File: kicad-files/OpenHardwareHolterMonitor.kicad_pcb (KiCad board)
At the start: 6 copper layers, 131 x 80 mm, 151 parts, among them CON1 Micro_SD_Card, J1 Conn_02x06_Odd_Even, J10 Conn_01x01, J11 Conn_01x01, J12 USB_OTG, J13 USB_C_Receptacle, J2 Conn_01x01, J3 Conn_01x01, J4 Conn_01x01, J5 Conn_01x01, J6 Conn_01x01, J7 Conn_01x01, J8 Conn_01x01, J9 Conn_01x01, P1 Custom_FTDI, Q1 S8050, Q10 Q_PMOS_DGS, Q2 S8050, Q3 Q_NMOS_DGS, Q4 Q_NMOS_DGS, Q5 Q_NMOS_DGS, Q6 Q_NMOS_DGS, Q7 Q_PMOS_DGS, Q8 Q_PMOS_DGS, Q9 Q_PMOS_DGS, SW1 SW_SPDT, U1 ESP-WROOM-32, U2 ADS1298, U3 MCP73833, U4 MCP73833, U5 TPS2113A, U6 LP5912, U7 REM_3-xxxxS, Y1 32768Hz

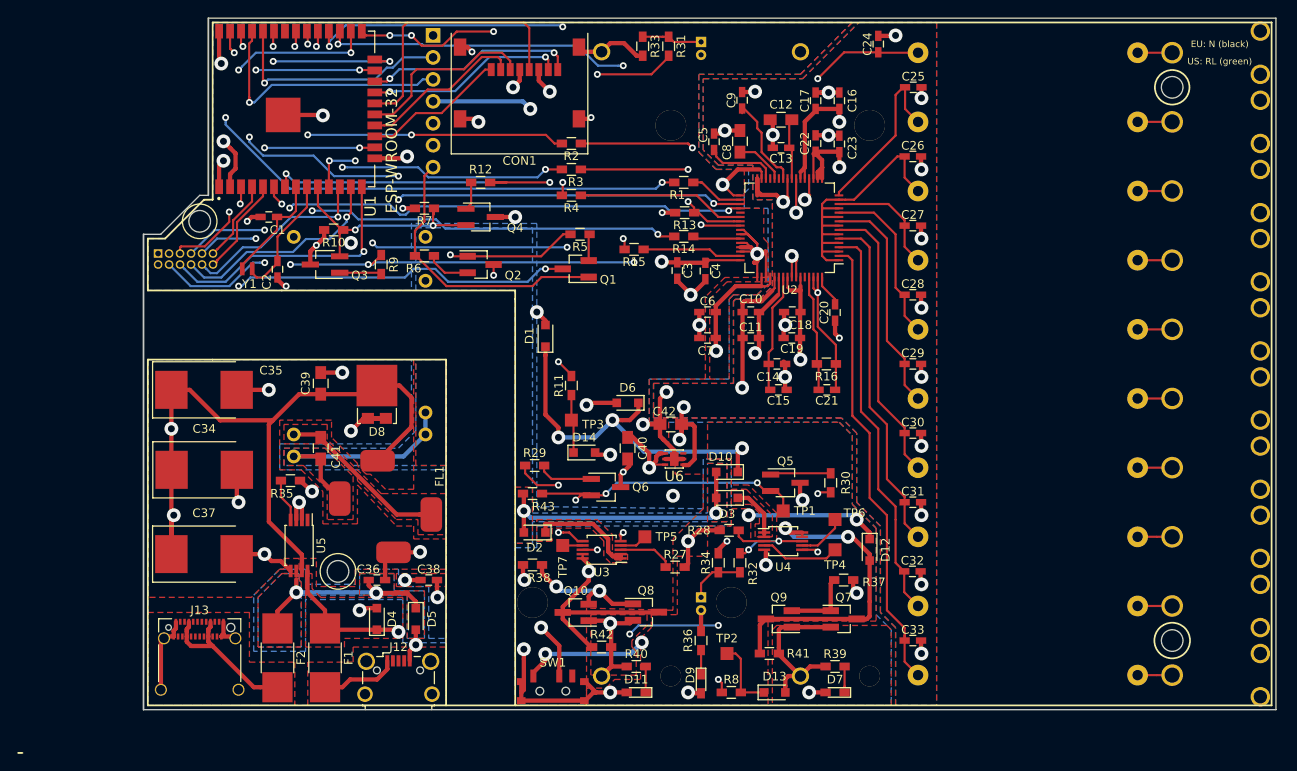
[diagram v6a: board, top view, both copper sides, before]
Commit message: DRC passes (with some missing courtyard warnings)
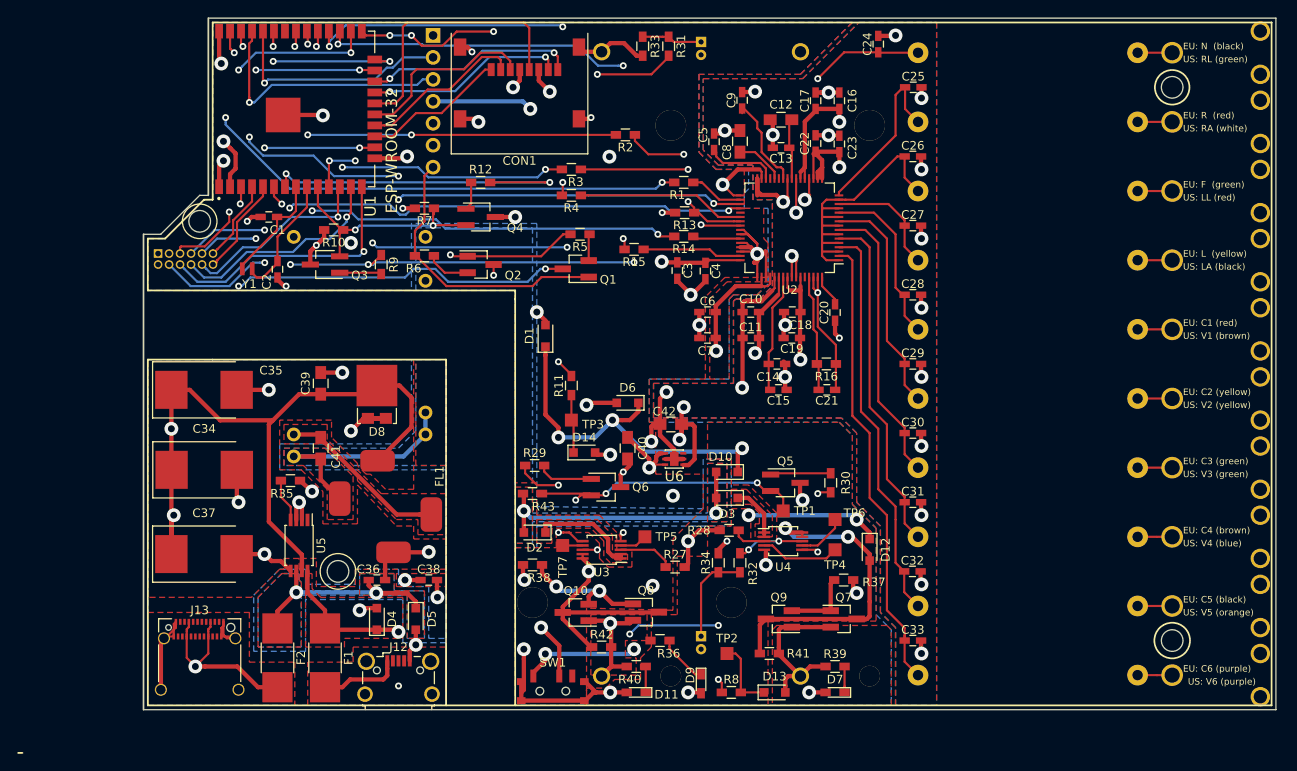
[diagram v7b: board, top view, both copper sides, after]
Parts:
- moved R2 6.33 mm to (194.8, 33.5)
- moved R36 4.75 mm to (198.8, 92.0), turned to 180 degrees
- moved TH2 4.50 mm to (203.5, 91.5)
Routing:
- net GND: track 211.8 -> 222.6 mm, vias 54 -> 56
- net GNDPWR: track 57.4 -> 64.0 mm
- net /ads1298/ADS_SCLK: track 27.0 -> 20.6 mm
- net /CLK: track 41.9 -> 47.7 mm
- net Net-(R32-Pad1): track 6.64 -> 11.1 mm
- net +5C: track 18.2 -> 22.1 mm, vias 0 -> 1
- net /read_bat_2: track 59.7 -> 62.8 mm
- net Net-(D9-Pad1): track 2.80 -> 5.82 mm
- net /power/USB_C_IN: track 23.5 -> 24.4 mm
- net Net-(D3-Pad1): track 6.18 -> 6.68 mm
- net +5V: track 9.03 -> 9.46 mm, vias 0 -> 1
- added copper zone on In2.Cu.power, net +5V
- added copper zone on In3.Cu.vert, net GND
- added copper zone on In3.Cu.vert, net GNDPWR
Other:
- net class Default: clearance 0.2 -> 0.13
- net class Power: clearance 0.2 -> 0.13
- rule trace_clearance: 0.2 -> 0.13
- board text added: "EU: C1 (red)"
- board text added: "EU: C2 (yellow)"
- board text added: "EU: C3 (green)"
- board text added: "EU: C4 (brown)"
- board text added: "EU: C5 (black)"
- board text added: "EU: C6 (purple)"
- board text added: "EU: F (green)"
- board text added: "EU: L (yellow)"
- board text added: "EU: R (red)"
- board text added: "US: LA (black)"
- board text added: "US: LL (red)"
- board text added: "US: RA (white)"
- board text added: "US: V1 (brown)"
- board text added: "US: V2 (yellow)"
- board text added: "US: V3 (green)"
- board text added: "US: V4 (blue)"
- board text added: "US: V5 (orange)"
- board text added: "US: V6 (purple)"

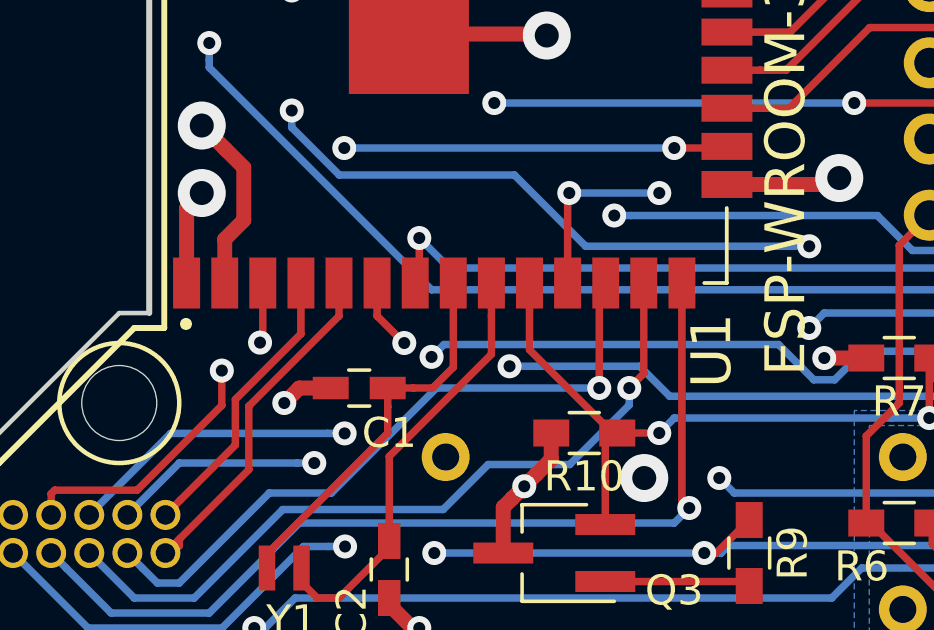
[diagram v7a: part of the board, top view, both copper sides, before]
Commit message: esp-wroom footprint update
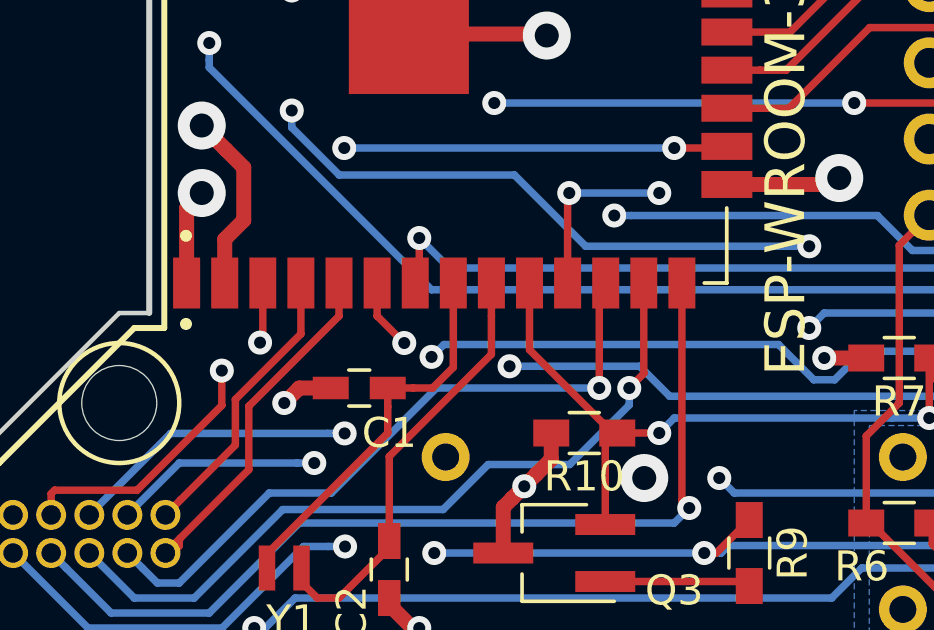
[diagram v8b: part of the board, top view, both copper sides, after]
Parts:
- U1: footprint ESP-WROOM-32:MODULE_ESP-WROOM-32_NO_SILK_ANTENNA -> esp-wroom-32:MODULE_ESP-WROOM-32
